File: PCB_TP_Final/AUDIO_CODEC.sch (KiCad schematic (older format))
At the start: 1 part, among them J1 Conn_01x09

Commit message: Add footprint CODEC_AUDIO_WM8731
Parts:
- J1: footprint (none) -> CUSTOM_LIB:Audio_Codec_WM8731
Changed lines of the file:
@@
 F 0 "J1" H 5800 3750 50  0000 C CNN
 F 1 "Conn_01x09" H 5800 2750 50  0000 C CNN
-F 2 "" H 5800 3250 50  0001 C CNN
+F 2 "CUSTOM_LIB:Audio_Codec_WM8731" H 5800 3250 50  0001 C CNN
 F 3 "" H 5800 3250 50  0001 C CNN
 	1    5800 3250

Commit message: Add 3D conections and NODEMCU ESP12
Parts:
- J1: footprint CUSTOM_LIB:Audio_Codec_WM8731 -> AUDIO_CODEC_WM8731:Audio_Codec_WM8731
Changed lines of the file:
@@
 LIBS:contrib
 LIBS:valves
+LIBS:nodemcu_esp12
 LIBS:PCB_TP_Final-cache
 EELAYER 25 0
@@
 $Descr A4 11693 8268
 encoding utf-8
-Sheet 2 2
+Sheet 2 3
 Title ""
 Date ""
@@
 F 0 "J1" H 5800 3750 50  0000 C CNN
 F 1 "Conn_01x09" H 5800 2750 50  0000 C CNN
-F 2 "CUSTOM_LIB:Audio_Codec_WM8731" H 5800 3250 50  0001 C CNN
+F 2 "AUDIO_CODEC_WM8731:Audio_Codec_WM8731" H 5800 3250 50  0001 C CNN
 F 3 "" H 5800 3250 50  0001 C CNN
 	1    5800 3250

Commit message: Primera entrega (1.0) para revision
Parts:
- added R1: 3.3K, Resistors_SMD:R_1206, symbol R
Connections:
- net MOSI: now also R1.1
- net +3V3 renamed 3.3VB
- net 3.3VB: now also R1.2
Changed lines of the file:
@@
 LIBS:valves
 LIBS:nodemcu_esp12
+LIBS:power_mb_v2
 LIBS:PCB_TP_Final-cache
 EELAYER 25 0
@@
 $Descr A4 11693 8268
 encoding utf-8
-Sheet 2 3
+Sheet 2 4
 Title ""
-Date ""
+Date "2018-09-26"
 Rev ""
 Comp ""
@@
 Text HLabel 5150 2950 0    60   Input ~ 0
 MISO
-Text HLabel 5150 3050 0    60   Input ~ 0
+Text HLabel 4050 3050 0    60   Input ~ 0
 MOSI
 Text HLabel 5150 3150 0    60   Input ~ 0
@@
 	5600 2950 5150 2950
 Wire Wire Line
-	5600 3050 5150 3050
+	5600 3050 4050 3050
 Wire Wire Line
 	5600 3150 5150 3150
@@
 	5600 3450 5150 3450
 $Comp
-L +3.3V #PWR03
-U 1 1 5BA5995E
-P 4550 3450
-F 0 "#PWR03" H 4550 3300 50  0001 C CNN
-F 1 "+3.3V" H 4550 3590 50  0000 C CNN
-F 2 "" H 4550 3450 50  0001 C CNN
-F 3 "" H 4550 3450 50  0001 C CNN
-	1    4550 3450
-	-1   0    0    -1
-$EndComp
-Wire Wire Line
-	5600 3550 4550 3550
-Wire Wire Line
-	4550 3550 4550 3450
-$Comp
-L GND #PWR04
+L GND #PWR02
 U 1 1 5BA59985
 P 4550 3750
-F 0 "#PWR04" H 4550 3500 50  0001 C CNN
+F 0 "#PWR02" H 4550 3500 50  0001 C CNN
 F 1 "GND" H 4550 3600 50  0000 C CNN
 F 2 "" H 4550 3750 50  0001 C CNN
@@
 Wire Wire Line
 	4550 3650 4550 3750
+Text GLabel 4050 3550 0    60   Input ~ 0
+3.3VB
+$Comp
+L R R1
+U 1 1 5BA9EB39
+P 4550 3300
+F 0 "R1" V 4630 3300 50  0000 C CNN
+F 1 "3.3K" V 4550 3300 50  0000 C CNN
+F 2 "Resistors_SMD:R_1206" V 4480 3300 50  0001 C CNN
+F 3 "" H 4550 3300 50  0001 C CNN
+	1    4550 3300
+	1    0    0    -1
+$EndComp
+Wire Wire Line
+	5600 3550 4050 3550
+Wire Wire Line
+	4550 3450 4550 3550
+Connection ~ 4550 3550
+Wire Wire Line
+	4550 3150 4550 3050
+Connection ~ 4550 3050
 $EndSCHEMATC

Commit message: Revisión 2.0 para evaluación
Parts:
- R1: footprint Resistors_SMD:R_1206 -> Resistors_SMD:R_1206_HandSoldering
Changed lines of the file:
@@
 $Descr A4 11693 8268
 encoding utf-8
-Sheet 2 4
+Sheet 2 5
 Title ""
 Date "2018-09-26"
@@
 	1    0    0    -1
 $EndComp
-Text HLabel 5150 2850 0    60   Input ~ 0
+Text HLabel 5150 2850 0    60   Output ~ 0
 SCK
 Wire Wire Line
@@
 Text HLabel 5150 2950 0    60   Input ~ 0
 MISO
-Text HLabel 4050 3050 0    60   Input ~ 0
+Text HLabel 4050 3050 0    60   Output ~ 0
 MOSI
-Text HLabel 5150 3150 0    60   Input ~ 0
+Text HLabel 5150 3150 0    60   Output ~ 0
 ADCL
-Text HLabel 5150 3250 0    60   Input ~ 0
+Text HLabel 5150 3250 0    60   Output ~ 0
 DACL
-Text HLabel 5150 3350 0    60   Input ~ 0
+Text HLabel 5150 3350 0    60   BiDi ~ 0
 SDA
-Text HLabel 5150 3450 0    60   Input ~ 0
+Text HLabel 5150 3450 0    60   Output ~ 0
 SCL
 Wire Wire Line
@@
 F 0 "R1" V 4630 3300 50  0000 C CNN
 F 1 "3.3K" V 4550 3300 50  0000 C CNN
-F 2 "Resistors_SMD:R_1206" V 4480 3300 50  0001 C CNN
+F 2 "Resistors_SMD:R_1206_HandSoldering" V 4480 3300 50  0001 C CNN
 F 3 "" H 4550 3300 50  0001 C CNN
 	1    4550 3300

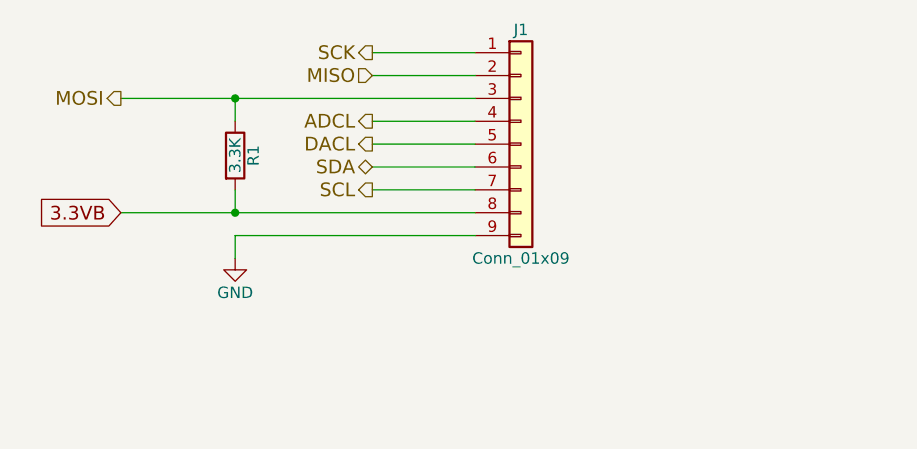
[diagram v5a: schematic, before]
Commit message: Se agregaron correcciones sugeridas
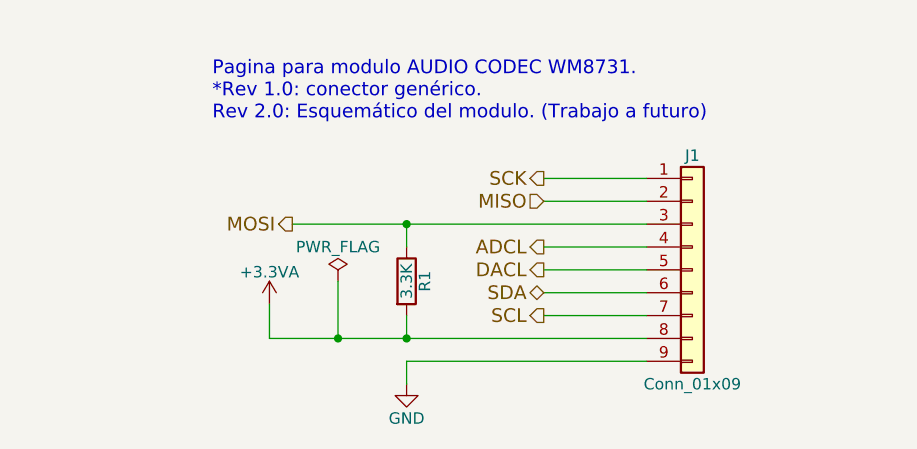
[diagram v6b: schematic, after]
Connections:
- net 3.3VB renamed +3.3VA
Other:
- note added: "Pagina para modulo AUDIO CODEC WM8731.\n*Rev 1.0: conector genérico.\nRev 2.0: Esquemático del modulo. (Trabajo a futuro)"
- moved on the sheet: J1, R1
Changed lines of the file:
@@
 encoding utf-8
 Sheet 2 5
-Title ""
-Date "2018-09-26"
-Rev ""
-Comp ""
+Title "Audio Codec WM8731"
+Date "2018-10-19"
+Rev "1.0"
+Comp "Ericson Joseph Estupiñan Pineda"
 Comment1 ""
 Comment2 ""
@@
 L Conn_01x09 J1
 U 1 1 5BA58F64
-P 5800 3250
-F 0 "J1" H 5800 3750 50  0000 C CNN
-F 1 "Conn_01x09" H 5800 2750 50  0000 C CNN
-F 2 "AUDIO_CODEC_WM8731:Audio_Codec_WM8731" H 5800 3250 50  0001 C CNN
-F 3 "" H 5800 3250 50  0001 C CNN
-	1    5800 3250
+P 6550 3800
+F 0 "J1" H 6550 4300 50  0000 C CNN
+F 1 "Conn_01x09" H 6550 3300 50  0000 C CNN
+F 2 "AUDIO_CODEC_WM8731:Audio_Codec_WM8731" H 6550 3800 50  0001 C CNN
+F 3 "" H 6550 3800 50  0001 C CNN
+	1    6550 3800
 	1    0    0    -1
 $EndComp
-Text HLabel 5150 2850 0    60   Output ~ 0
+Text HLabel 5900 3400 0    60   Output ~ 0
 SCK
 Wire Wire Line
-	5600 2850 5150 2850
-Text HLabel 5150 2950 0    60   Input ~ 0
+	6350 3400 5900 3400
+Text HLabel 5900 3500 0    60   Input ~ 0
 MISO
-Text HLabel 4050 3050 0    60   Output ~ 0
+Text HLabel 4800 3600 0    60   Output ~ 0
 MOSI
-Text HLabel 5150 3150 0    60   Output ~ 0
+Text HLabel 5900 3700 0    60   Output ~ 0
 ADCL
-Text HLabel 5150 3250 0    60   Output ~ 0
+Text HLabel 5900 3800 0    60   Output ~ 0
 DACL
-Text HLabel 5150 3350 0    60   BiDi ~ 0
+Text HLabel 5900 3900 0    60   BiDi ~ 0
 SDA
-Text HLabel 5150 3450 0    60   Output ~ 0
+Text HLabel 5900 4000 0    60   Output ~ 0
 SCL
 Wire Wire Line
-	5600 2950 5150 2950
+	6350 3500 5900 3500
 Wire Wire Line
-	5600 3050 4050 3050
+	6350 3600 4800 3600
 Wire Wire Line
-	5600 3150 5150 3150
+	6350 3700 5900 3700
 Wire Wire Line
-	5600 3250 5150 3250
+	6350 3800 5900 3800
 Wire Wire Line
-	5600 3350 5150 3350
+	6350 3900 5900 3900
 Wire Wire Line
-	5600 3450 5150 3450
+	6350 4000 5900 4000
 $Comp
-L GND #PWR03
+L GND #PWR04
 U 1 1 5BA59985
-P 4550 3750
-F 0 "#PWR03" H 4550 3500 50  0001 C CNN
-F 1 "GND" H 4550 3600 50  0000 C CNN
-F 2 "" H 4550 3750 50  0001 C CNN
-F 3 "" H 4550 3750 50  0001 C CNN
-	1    4550 3750
+P 5300 4300
+F 0 "#PWR04" H 5300 4050 50  0001 C CNN
+F 1 "GND" H 5300 4150 50  0000 C CNN
+F 2 "" H 5300 4300 50  0001 C CNN
+F 3 "" H 5300 4300 50  0001 C CNN
+	1    5300 4300
 	1    0    0    -1
 $EndComp
 Wire Wire Line
-	5600 3650 4550 3650
+	6350 4200 5300 4200
 Wire Wire Line
-	4550 3650 4550 3750
-Text GLabel 4050 3550 0    60   Input ~ 0
-3.3VB
+	5300 4200 5300 4300
 $Comp
 L R R1
 U 1 1 5BA9EB39
-P 4550 3300
-F 0 "R1" V 4630 3300 50  0000 C CNN
-F 1 "3.3K" V 4550 3300 50  0000 C CNN
-F 2 "Resistors_SMD:R_1206_HandSoldering" V 4480 3300 50  0001 C CNN
-F 3 "" H 4550 3300 50  0001 C CNN
-	1    4550 3300
+P 5300 3850
+F 0 "R1" V 5380 3850 50  0000 C CNN
+F 1 "3.3K" V 5300 3850 50  0000 C CNN
+F 2 "Resistors_SMD:R_1206_HandSoldering" V 5230 3850 50  0001 C CNN
+F 3 "" H 5300 3850 50  0001 C CNN
+	1    5300 3850
 	1    0    0    -1
 $EndComp
 Wire Wire Line
-	5600 3550 4050 3550
+	5300 3700 5300 3600
+Connection ~ 5300 3600
+$Comp
+L +3.3VA #PWR05
+U 1 1 5BCA7F4D
+P 4700 3950
+F 0 "#PWR05" H 4700 3800 50  0001 C CNN
+F 1 "+3.3VA" H 4700 4090 50  0000 C CNN
+F 2 "" H 4700 3950 50  0001 C CNN
+F 3 "" H 4700 3950 50  0001 C CNN
+	1    4700 3950
+	1    0    0    -1
+$EndComp
 Wire Wire Line
-	4550 3450 4550 3550
-Connection ~ 4550 3550
+	6350 4100 4700 4100
 Wire Wire Line
-	4550 3150 4550 3050
-Connection ~ 4550 3050
+	4700 4100 4700 3950
+Wire Wire Line
+	5300 4000 5300 4100
+Connection ~ 5300 4100
+$Comp
+L PWR_FLAG #FLG06
+U 1 1 5BCA8A79
+P 5000 3850
+F 0 "#FLG06" H 5000 3925 50  0001 C CNN
+F 1 "PWR_FLAG" H 5000 4000 50  0000 C CNN
+F 2 "" H 5000 3850 50  0001 C CNN
+F 3 "" H 5000 3850 50  0001 C CNN
+	1    5000 3850
+	1    0    0    -1
+$EndComp
+Wire Wire Line
+	5000 3850 5000 4100
+Connection ~ 5000 4100
+Text Notes 4450 3150 0    60   ~ 0
+Pagina para modulo AUDIO CODEC WM8731.\n*Rev 1.0: conector genérico.\nRev 2.0: Esquemático del modulo. (Trabajo a futuro)
 $EndSCHEMATC
